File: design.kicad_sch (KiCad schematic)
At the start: 14 parts, among them J1 Conn_01x06_Male, U1 IQS231A-00000000-TSR

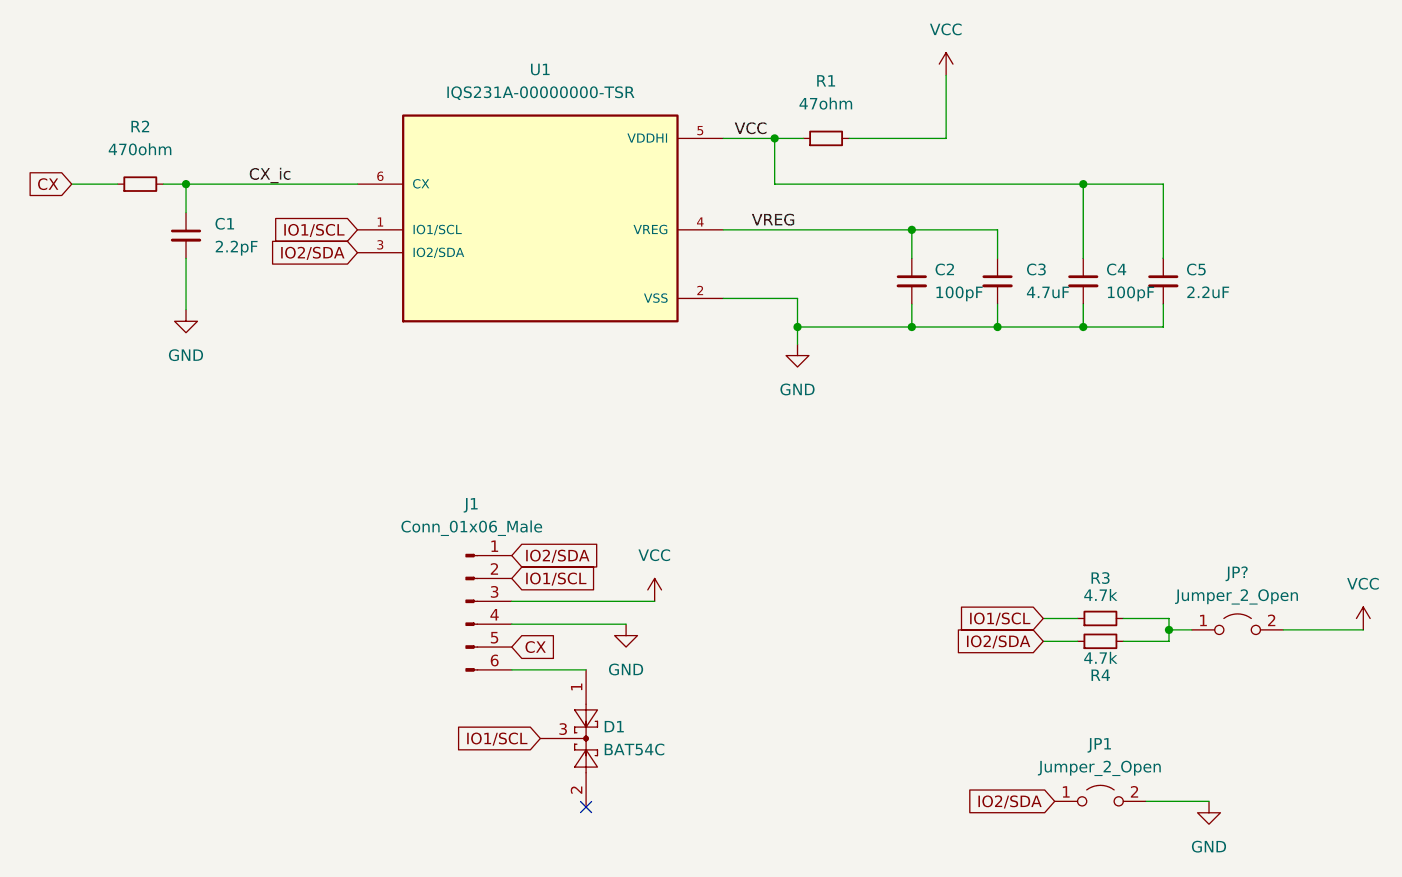
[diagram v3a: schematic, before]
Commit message: add groundplane and DRC/ERC
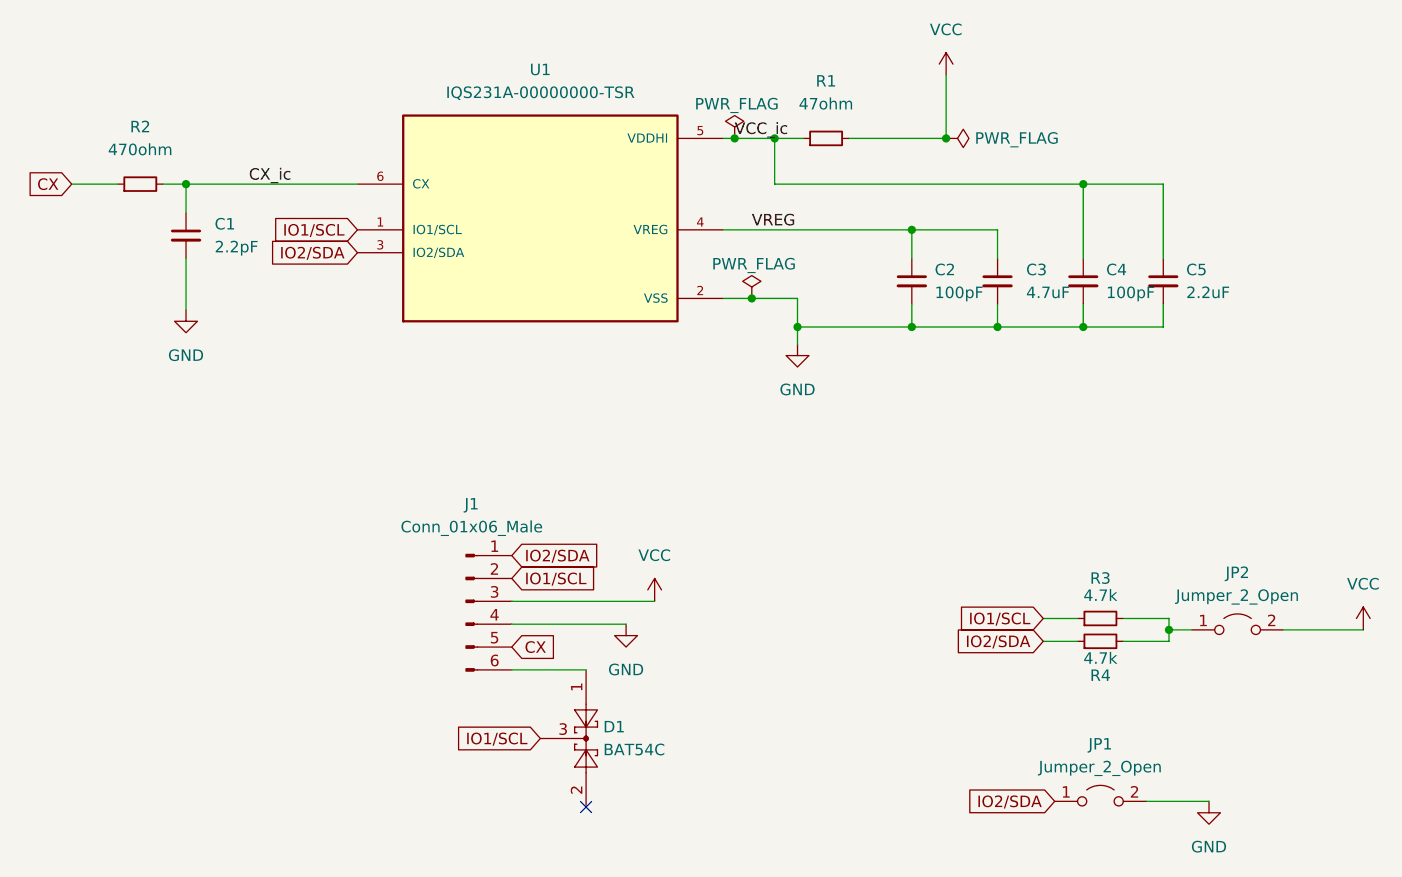
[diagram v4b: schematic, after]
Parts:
- gave numbers to parts that had none: 1
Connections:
- net VCC: no longer C4.1, C5.1, R1.1, U1.5 (VDDHI)
- new net VCC_ic: C4.1, C5.1, R1.1, U1.5 (VDDHI)
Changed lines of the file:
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@@
   (junction (at 189.23 83.82) (diameter 0) (color 0 0 0 0)
   )
+  (junction (at 169.545 73.66) (diameter 0) (color 0 0 0 0)
+  )
   (junction (at 198.755 94.615) (diameter 0) (color 0 0 0 0)
   )
@@
   )
   (junction (at 217.805 128.27) (diameter 0) (color 0 0 0 0)
+  )
+  (junction (at 193.04 73.66) (diameter 0) (color 0 0 0 0)
+  )
+  (junction (at 171.45 91.44) (diameter 0) (color 0 0 0 0)
   )
   (no_connect (at 153.035 147.955))
@@
     (stroke (width 0) (type default) (color 0 0 0 0))
   )
+  (wire (pts (xy 171.45 91.44) (xy 176.53 91.44))
+    (stroke (width 0) (type default) (color 0 0 0 0))
+  )
   (wire (pts (xy 212.725 129.54) (xy 217.805 129.54))
     (stroke (width 0) (type default) (color 0 0 0 0))
@@
     (stroke (width 0) (type default) (color 0 0 0 0))
   )
-  (wire (pts (xy 168.275 73.66) (xy 173.99 73.66))
-    (stroke (width 0) (type default) (color 0 0 0 0))
-  )
   (wire (pts (xy 208.28 86.995) (xy 208.28 78.74))
     (stroke (width 0) (type default) (color 0 0 0 0))
@@
     (stroke (width 0) (type default) (color 0 0 0 0))
   )
-  (wire (pts (xy 168.275 91.44) (xy 176.53 91.44))
+  (wire (pts (xy 168.275 91.44) (xy 171.45 91.44))
     (stroke (width 0) (type default) (color 0 0 0 0))
   )
@@
     (stroke (width 0) (type default) (color 0 0 0 0))
   )
+  (wire (pts (xy 168.275 73.66) (xy 169.545 73.66))
+    (stroke (width 0) (type default) (color 0 0 0 0))
+  )
   (wire (pts (xy 95.885 78.74) (xy 100.965 78.74))
     (stroke (width 0) (type default) (color 0 0 0 0))
@@
     (stroke (width 0) (type default) (color 0 0 0 0))
   )
-  (label "VCC" (at 169.545 73.66 0)
+  (wire (pts (xy 169.545 73.66) (xy 173.99 73.66))
+    (stroke (width 0) (type default) (color 0 0 0 0))
+  )
+  (label "VCC_ic" (at 169.545 73.66 0)
     (effects (font (size 1.27 1.27)) (justify left bottom))
   )
@@
     (pin "2")
   )
+  (symbol (lib_id "power:PWR_FLAG") (at 169.545 73.66 0) (unit 1)
+    (in_bom yes) (on_board yes)
+    (property "Reference" "#FLG0102" (id 0) (at 169.545 71.755 0)
+      (effects (font (size 1.27 1.27)) hide)
+    )
+    (property "Value" "PWR_FLAG" (id 1) (at 165.1 69.85 0)
+      (effects (font (size 1.27 1.27)) (justify left))
+    )
+    (property "Footprint" "" (id 2) (at 169.545 73.66 0)
+      (effects (font (size 1.27 1.27)) hide)
+    )
+    (property "Datasheet" "~" (id 3) (at 169.545 73.66 0)
+      (effects (font (size 1.27 1.27)) hide)
+    )
+    (pin "1")
+  )
   (symbol (lib_id "power:VCC") (at 160.655 125.095 0) (unit 1)
     (in_bom yes) (on_board yes) (fields_autoplaced)
@@
   (symbol (lib_id "Jumper:Jumper_2_Open") (at 225.425 128.27 0) (unit 1)
     (in_bom yes) (on_board yes) (fields_autoplaced)
-    (property "Reference" "JP?" (id 0) (at 225.425 121.92 0))
+    (property "Reference" "JP2" (id 0) (at 225.425 121.92 0))
     (property "Value" "Jumper_2_Open" (id 1) (at 225.425 124.46 0))
     (property "Footprint" "Connector_PinHeader_2.54mm:PinHeader_1x02_P2.54mm_Vertical" (id 2) (at 225.425 128.27 0)
@@
     (pin "1")
     (pin "2")
+  )
+  (symbol (lib_id "power:PWR_FLAG") (at 171.45 91.44 0) (unit 1)
+    (in_bom yes) (on_board yes)
+    (property "Reference" "#FLG0103" (id 0) (at 171.45 89.535 0)
+      (effects (font (size 1.27 1.27)) hide)
+    )
+    (property "Value" "PWR_FLAG" (id 1) (at 167.005 87.63 0)
+      (effects (font (size 1.27 1.27)) (justify left))
+    )
+    (property "Footprint" "" (id 2) (at 171.45 91.44 0)
+      (effects (font (size 1.27 1.27)) hide)
+    )
+    (property "Datasheet" "~" (id 3) (at 171.45 91.44 0)
+      (effects (font (size 1.27 1.27)) hide)
+    )
+    (pin "1")
   )
   (symbol (lib_id "Device:C_Small") (at 208.28 89.535 0) (unit 1)
@@
     (pin "2")
   )
+  (symbol (lib_id "power:PWR_FLAG") (at 193.04 73.66 270) (unit 1)
+    (in_bom yes) (on_board yes) (fields_autoplaced)
+    (property "Reference" "#FLG0101" (id 0) (at 194.945 73.66 0)
+      (effects (font (size 1.27 1.27)) hide)
+    )
+    (property "Value" "PWR_FLAG" (id 1) (at 196.215 73.6599 90)
+      (effects (font (size 1.27 1.27)) (justify left))
+    )
+    (property "Footprint" "" (id 2) (at 193.04 73.66 0)
+      (effects (font (size 1.27 1.27)) hide)
+    )
+    (property "Datasheet" "~" (id 3) (at 193.04 73.66 0)
+      (effects (font (size 1.27 1.27)) hide)
+    )
+    (pin "1")
+  )
   (symbol (lib_id "Device:C_Small") (at 198.755 89.535 0) (unit 1)
     (in_bom yes) (on_board yes) (fields_autoplaced)
@@
   )
   (symbol_instances
+    (path "/f48ddda0-1405-4787-a101-3f610006b030"
+      (reference "#FLG0101") (unit 1) (value "PWR_FLAG") (footprint "")
+    )
+    (path "/3cad977d-8b2b-47b1-9a1d-3d955000f5da"
+      (reference "#FLG0102") (unit 1) (value "PWR_FLAG") (footprint "")
+    )
+    (path "/814396dc-eb73-4d8a-8a40-03fe54ca7369"
+      (reference "#FLG0103") (unit 1) (value "PWR_FLAG") (footprint "")
+    )
     (path "/e5573ba3-30bb-49f9-8338-4fc891a48d78"
       (reference "#PWR0101") (unit 1) (value "GND") (footprint "")
@@
     )
     (path "/7e065482-e9cb-4feb-8a5e-8a895d9ca9d6"
-      (reference "JP?") (unit 1) (value "Jumper_2_Open") (footprint "Connector_PinHeader_2.54mm:PinHeader_1x02_P2.54mm_Vertical")
+      (reference "JP2") (unit 1) (value "Jumper_2_Open") (footprint "Connector_PinHeader_2.54mm:PinHeader_1x02_P2.54mm_Vertical")
     )
     (path "/1ee4c7b2-34da-493e-abfd-70692e4ef9ad"
